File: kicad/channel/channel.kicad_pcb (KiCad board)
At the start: 2 copper layers, 49.5 x 24.8 mm, 38 parts, among them J1 Conn_01x07_Male, J2 Conn_01x01_Male, J3 Conn_01x01_Male, J4 Conn_01x01_Male, J5 Conn_01x01_Male, Q1 BC846B, Q2 IRF3205, Q3 IRF3205, Q4 BC846B, Q5 IRF3205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

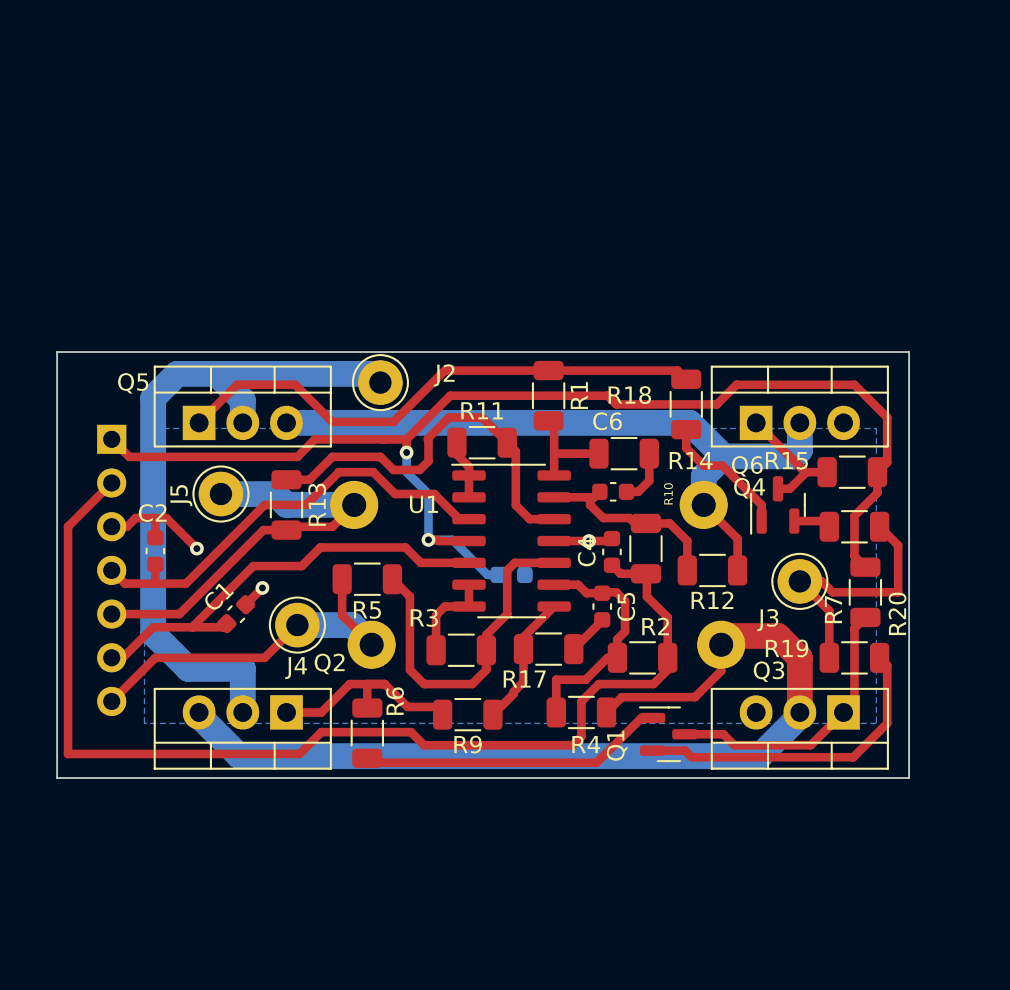
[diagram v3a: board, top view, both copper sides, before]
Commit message: fix flash, fix frequency compensation
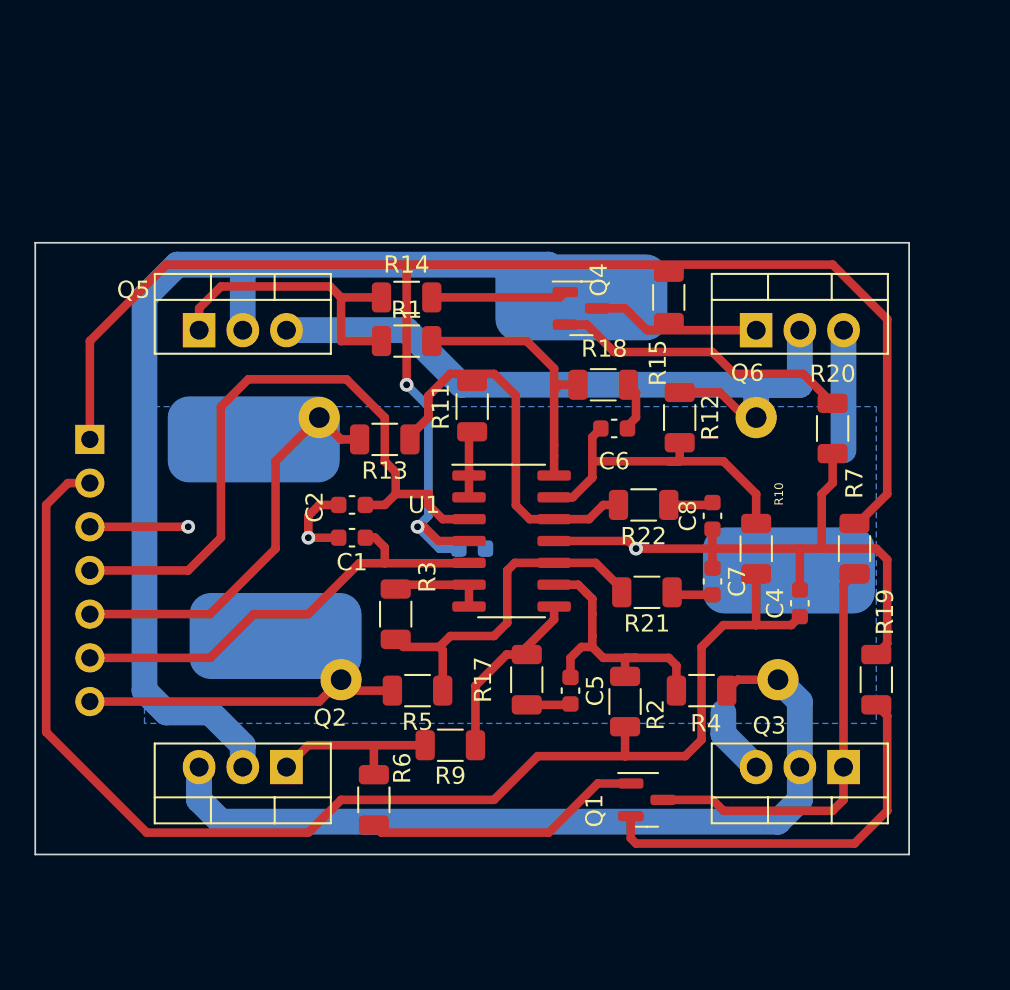
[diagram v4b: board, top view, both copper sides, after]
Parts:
- removed J2, J3, J5: Conn_01x01_Male, Connector_Pin:Pin_D1.3mm_L11.0mm
- added C7: 1u, Capacitor_SMD:C_0603_1608Metric, F.Cu at (171.4, 97.2)
- added C8: 1u, Capacitor_SMD:C_0603_1608Metric, F.Cu at (171.4, 93.3)
- added J5V1: Conn_01x01_Male, Channel:PowerPad, B.Cu at (163.8, 80.6)
- added JBat1: Conn_01x01_Male, Channel:PowerPad, B.Cu at (144.8, 88.9)
- added JGND1: Conn_01x01_Male, Channel:PowerPad, B.Cu at (175.9, 96.5)
- added R21: 22k, Resistor_SMD:R_1206_3216Metric, F.Cu at (167.6, 97.8)
- added R22: 22k, Resistor_SMD:R_1206_3216Metric, F.Cu at (167.4, 92.7)
- JBat2: renamed from J4; footprint Connector_Pin:Pin_D1.3mm_L11.0mm -> Channel:PowerPad; moved to B.Cu
- R16, R8: footprint Resistor_THT:R_Axial_DIN0614_L14.3mm_D5.7mm_P20.32mm_Horizontal -> Resistor_THT:R_Axial_DIN0617_L17.0mm_D6.0mm_P25.40mm_Horizontal
- R17, R18: value 10k -> 22k
- moved R14 17.4 mm to (153.7, 80.6), turned to 180 degrees
- moved Q4 16.2 mm to (163.8, 81.3), turned to 0 degrees
- moved R15 14.7 mm to (168.9, 80.6), turned to 90 degrees
- moved C2 11.7 mm to (150.5, 92.7), turned to 180 degrees
- moved C4 11.3 mm to (176.5, 98.4)
- moved R12 9.09 mm to (169.5, 87.6), turned to 90 degrees
- moved R1 8.84 mm to (153.7, 83.2), turned to 0 degrees
- moved C1 8.07 mm to (150.5, 94.6), turned to 180 degrees
- moved R5 7.11 mm to (154.3, 103.5)
- moved R4 7.10 mm to (170.8, 103.5)
- moved R13 6.87 mm to (152.4, 88.9), turned to 180 degrees
- moved R10 6.41 mm to (174.0, 95.2)
- moved R16 5.92 mm to (174.0, 87.6)
- moved R20 5.85 mm to (178.4, 88.3), turned to 90 degrees
- moved Q5 5.39 mm to (141.6, 82.5)
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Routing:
- net GND: track 27.2 -> 58.4 mm
- net +5V: track 39.8 -> 61.3 mm
- net +12V: track 72.0 -> 90.3 mm
- net Net-(Q4-Pad2): track 2.17 -> 17.4 mm
- net Net-(Q5-Pad1): track 31.6 -> 17.5 mm
- net IN1: track 26.1 -> 39.1 mm
- net ref: track 63.8 -> 75.6 mm
- net Net-(R1-Pad2): track 5.96 -> 15.5 mm
- net Net-(Q1-Pad3): track 16.3 -> 24.4 mm
- net Net-(C6-Pad1): track 12.1 -> 19.5 mm
- net Net-(Q2-Pad3): track 54.9 -> 48.6 mm
- net Net-(Q1-Pad2): track 18.6 -> 23.5 mm
- net Net-(Q5-Pad3): track 40.3 -> 43.8 mm
- net Net-(R17-Pad1): track 7.76 -> 10.6 mm
- net Net-(C5-Pad1): track 13.9 -> 16.5 mm
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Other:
- board size 49.5 x 24.8 mm -> 50.8 x 35.6 mm

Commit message: add resistor matching
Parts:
- moved R6 5.08 mm to (156.8, 109.9)
- moved R14 4.45 mm to (158.1, 80.6)
- moved R9 3.81 mm to (152.4, 106.7)
- moved R15 0.63 mm to (168.9, 80.0)
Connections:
- R14 pad 2: Net-(Q5-Pad1) -> Net-(R1-Pad2)
- R6 pad 2: Net-(Q2-Pad1) -> Net-(R17-Pad1)
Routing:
- net Net-(Q2-Pad1): track 10.3 -> 4.78 mm
- net Net-(R17-Pad1): track 10.6 -> 15.9 mm
- net Net-(Q1-Pad1): track 16.3 -> 11.2 mm
- net Net-(Q4-Pad1): track 7.89 -> 3.45 mm
- net Net-(R1-Pad2): track 15.5 -> 18.5 mm
- net +12V: track 90.3 -> 92.9 mm
- net Net-(Q5-Pad1): track 17.5 -> 15.2 mm

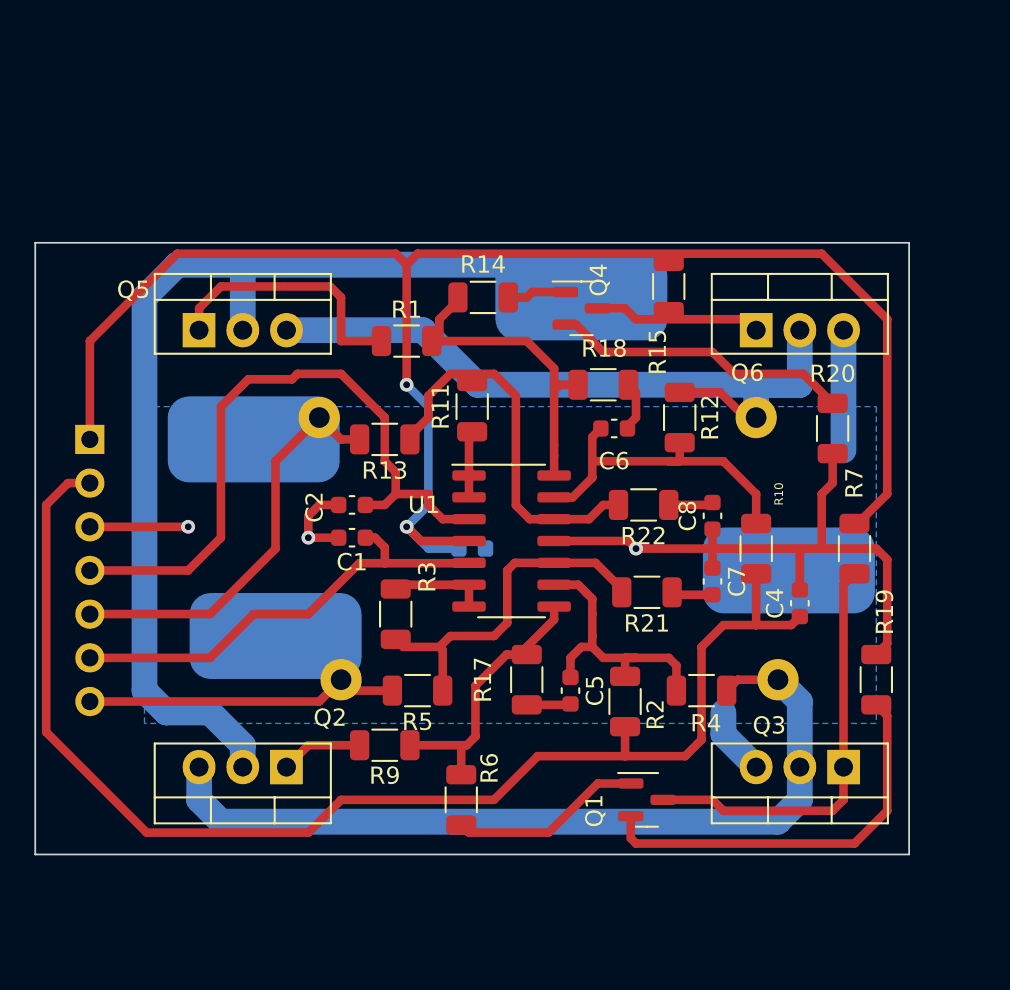
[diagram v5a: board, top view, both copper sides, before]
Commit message: move mosfets
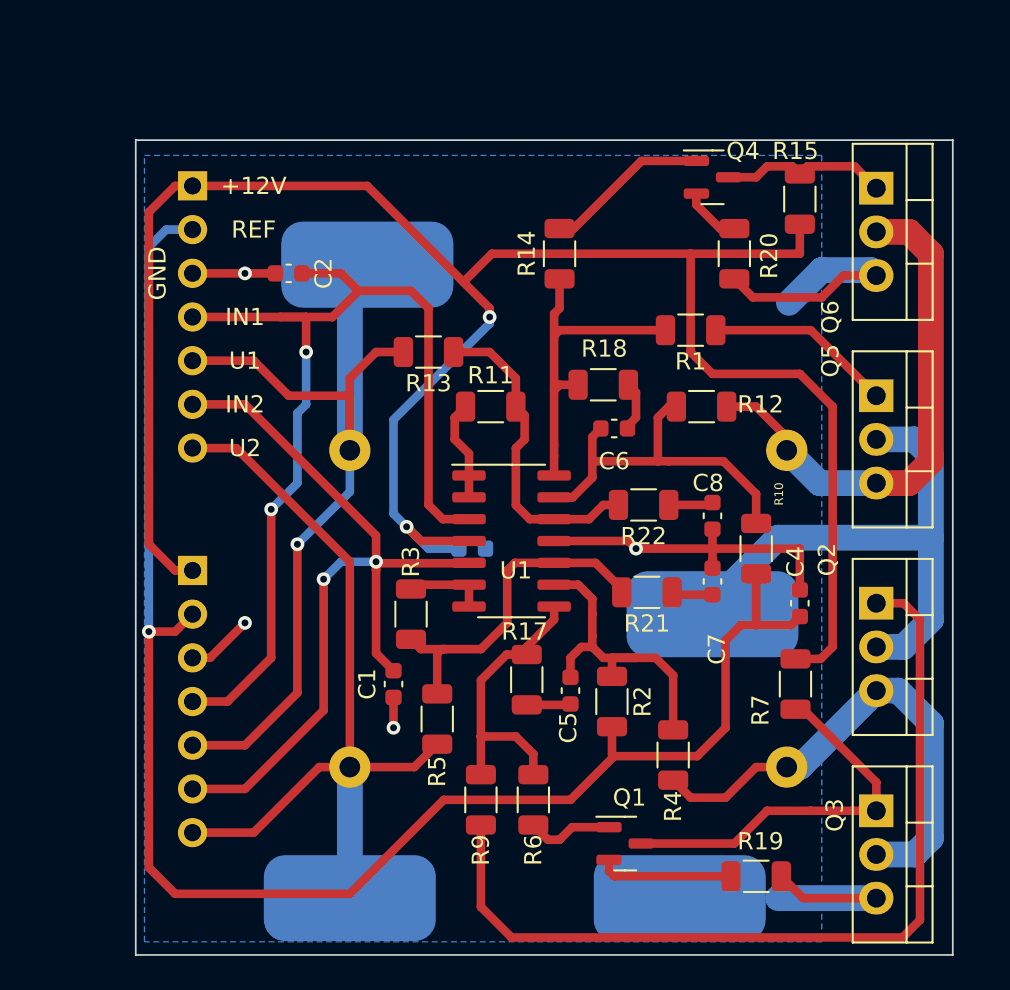
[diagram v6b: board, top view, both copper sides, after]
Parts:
- added J2: Conn_01x07_Male, Connector_PinHeader_2.54mm:PinHeader_1x07_P2.54mm_Vertical, B.Cu at (141.2, 96.5)
- moved Q5 39.6 mm to (181.0, 86.4), turned to -90 degrees
- moved Q2 35.6 mm to (181.0, 98.4), turned to -90 degrees
- moved JGND1 20.1 mm to (169.5, 115.6)
- moved J5V1 19.9 mm to (171.4, 99.1)
- moved R1 16.5 mm to (170.2, 82.5), turned to 180 degrees
- moved J1 15.9 mm to (141.2, 74.2)
- moved JBat2 15.8 mm to (150.4, 115.6)
- moved C2 14.0 mm to (146.8, 79.2)
- moved R19 13.4 mm to (174.0, 114.3), turned to 180 degrees
- moved JBat1 12.1 mm to (151.4, 78.7), turned to 0 degrees
- moved R20 11.7 mm to (172.7, 78.1)
- moved Q6 10.8 mm to (181.0, 74.3), turned to -90 degrees
- moved Q4 10.8 mm to (171.4, 73.7)
- moved R15 9.16 mm to (176.5, 74.9), turned to -90 degrees
- moved C1 8.84 mm to (152.9, 103.1), turned to -90 degrees
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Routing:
- net Net-(Q2-Pad1): track 4.78 -> 51.8 mm
- net U1: track 23.9 -> 55.0 mm, vias 0 -> 1
- net +12V: track 92.9 -> 122.4 mm
- net +5V: track 61.3 -> 31.8 mm
- net U2: track 23.2 -> 47.8 mm
- net IN2: track 26.6 -> 48.5 mm, vias 0 -> 2
- net IN1: track 39.4 -> 60.4 mm, vias 0 -> 2
- net Net-(Q2-Pad3): track 48.6 -> 29.0 mm
- net ref: track 75.6 -> 94.9 mm, vias 0 -> 1
- net Net-(Q1-Pad2): track 23.5 -> 7.87 mm
- net Net-(Q4-Pad2): track 17.4 -> 3.43 mm
- net Net-(Q5-Pad3): track 43.8 -> 30.5 mm
- net Net-(Q1-Pad1): track 11.2 -> 5.05 mm
- net Net-(Q4-Pad1): track 3.45 -> 9.58 mm
- net Net-(Q5-Pad1): track 15.2 -> 10.9 mm
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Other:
- board size 50.8 x 35.6 mm -> 47.5 x 47.4 mm
- board text added: "REF"
- board text removed: "ref"
